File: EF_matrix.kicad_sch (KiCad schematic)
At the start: 4 parts, among them J2 Conn_02x05_Counter_Clockwise, U5 ESP32_NODEMCU

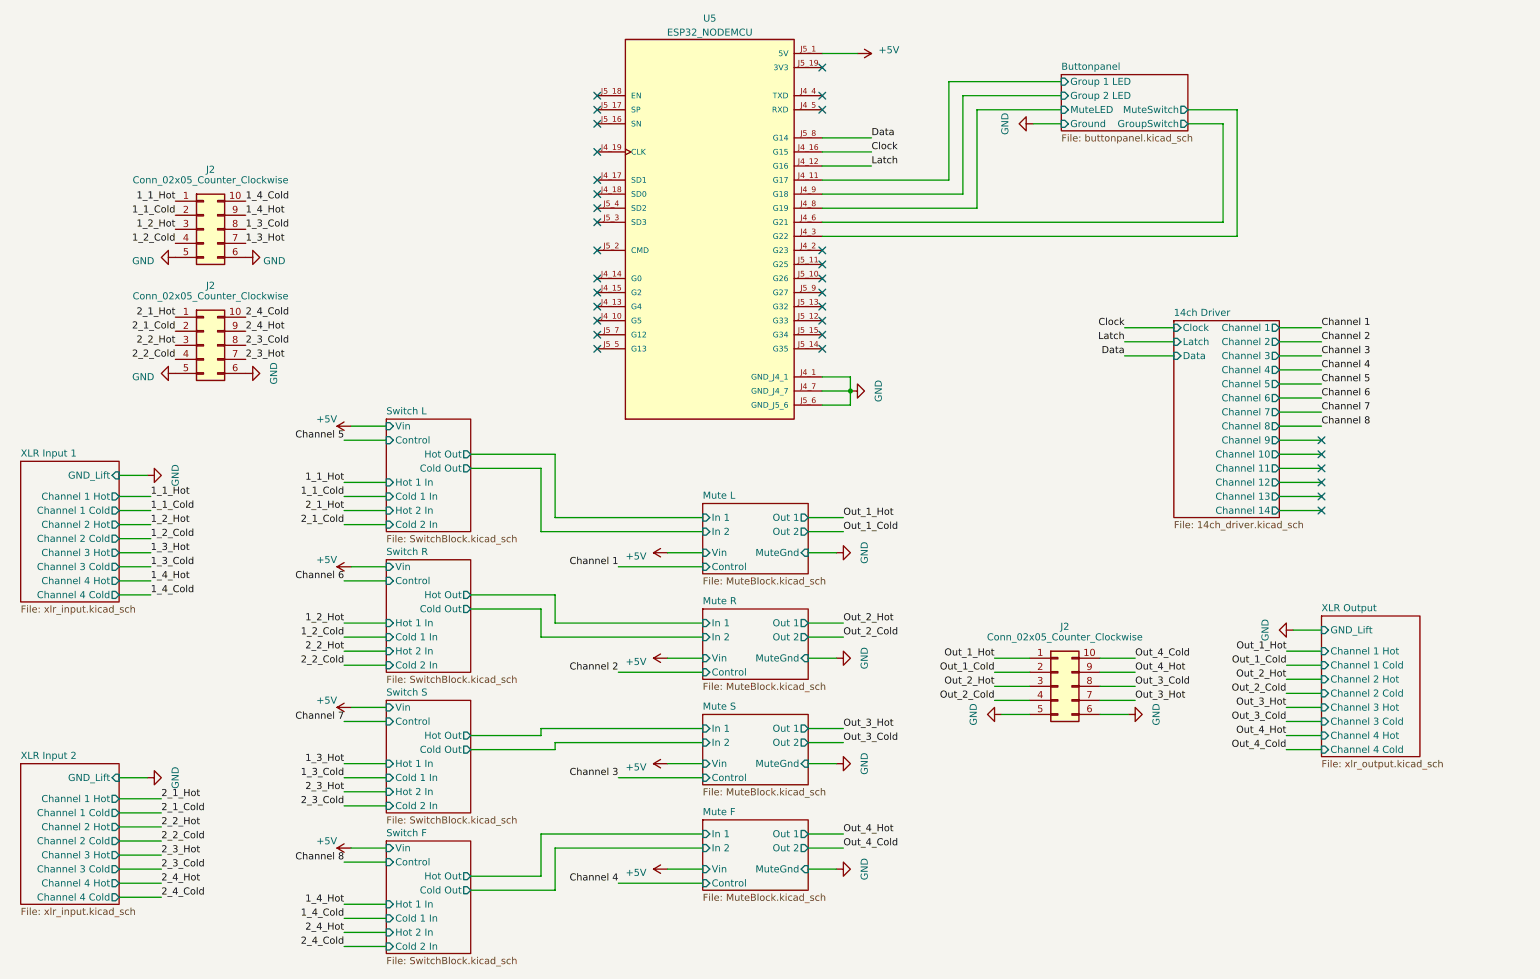
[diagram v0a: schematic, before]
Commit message: Finished up schematic, before board splitting
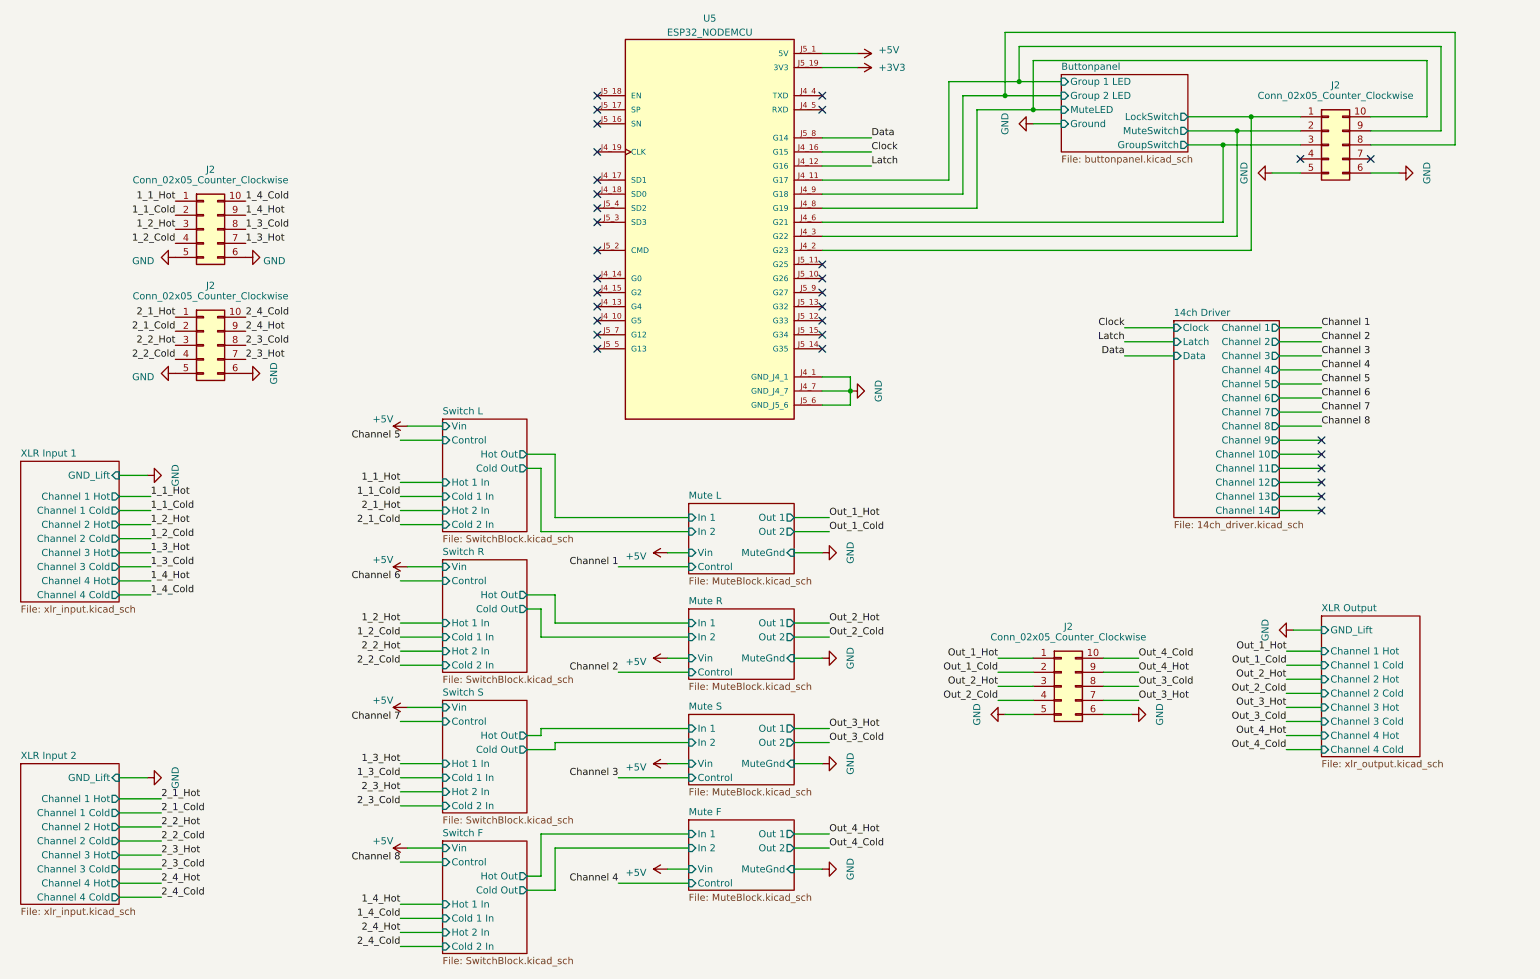
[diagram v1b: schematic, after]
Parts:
- added J2: Conn_02x05_Counter_Clockwise, Connector_PinSocket_2.54mm:PinSocket_2x05_P2.54mm_Vertical, symbol Connector_Generic:Conn_02x05_Counter_Clockwise
- J2: footprint (none) -> Connector_PinSocket_2.54mm:PinSocket_2x05_P2.54mm_Vertical
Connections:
- net Buttonpanel/Group 1 LED: now also J2.9 (Pin_9)
- net Buttonpanel/Group 2 LED: now also J2.8 (Pin_8)
- net Buttonpanel/GroupSwitch: now also J2.3 (Pin_3)
- net Buttonpanel/MuteLED: now also J2.10 (Pin_10)
- net Buttonpanel/MuteSwitch: now also J2.2 (Pin_2)
- net GND: now also J2.5 (Pin_5), J2.6 (Pin_6)
- net Buttonpanel/LockSwitch: now reaches U5.J4_2 (G23)
- net Buttonpanel/LockSwitch: now also J2.1 (Pin_1)
- net +3V3: now reaches U5.J5_19 (3V3)
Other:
- sheet Buttonpanel ports: added LockSwitch; removed none
- moved on the sheet: J2

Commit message: Changed position of ribbon connectors, added DC
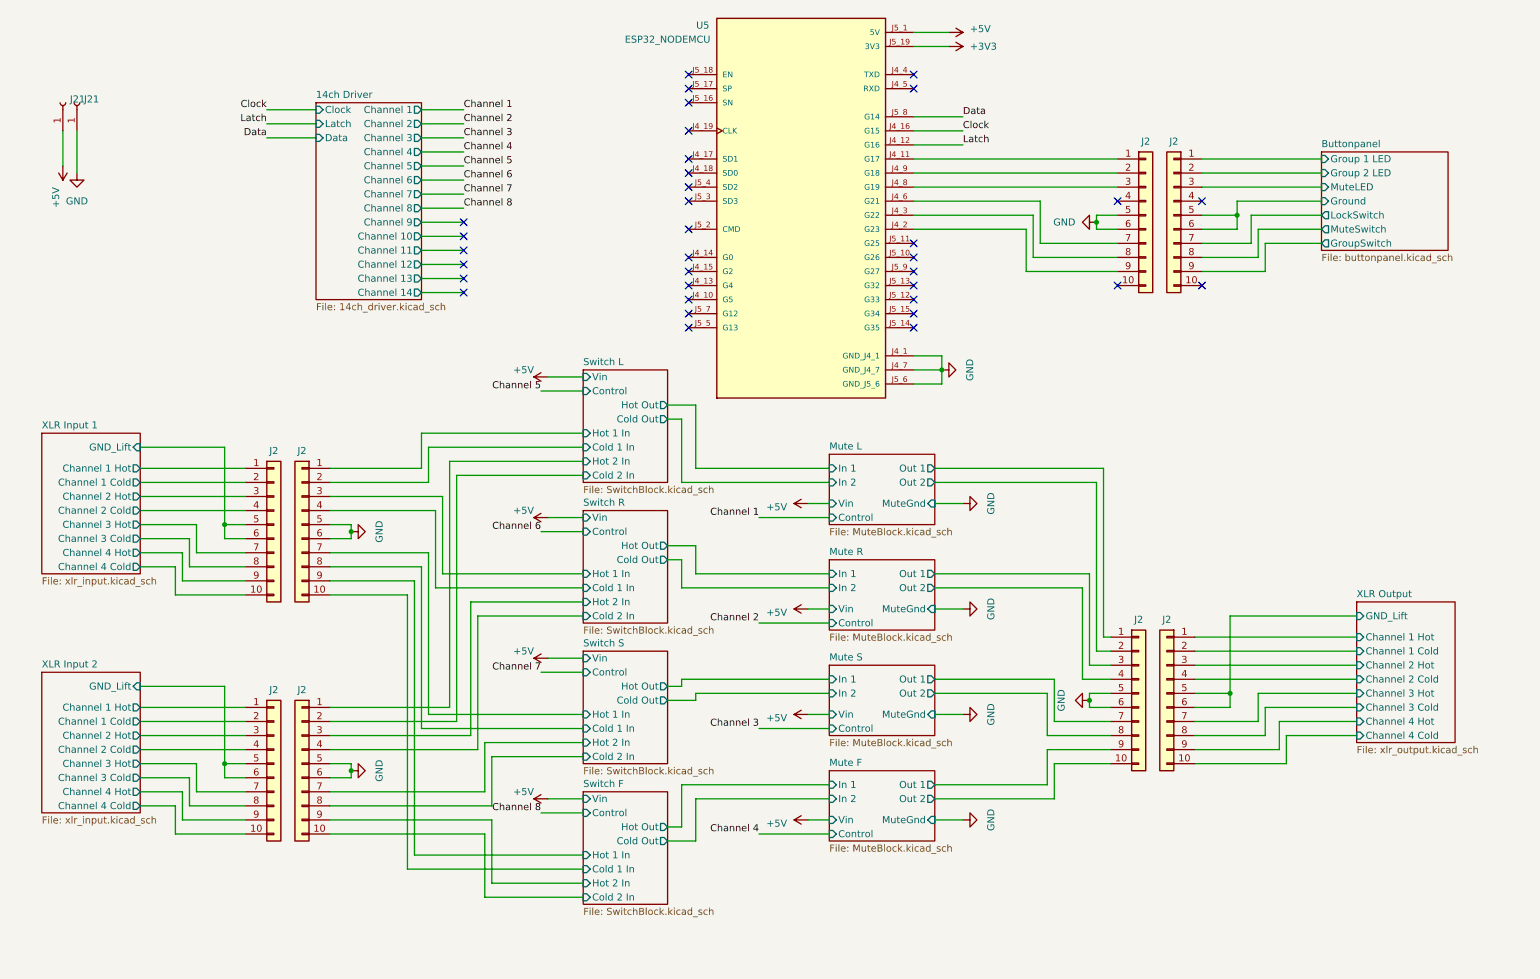
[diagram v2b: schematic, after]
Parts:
- removed J2 (x3): Conn_02x05_Counter_Clockwise, Connector_PinSocket_2.54mm:PinSocket_2x05_P2.54mm_Vertical, symbol Connector_Generic:Conn_02x05_Counter_Clockwise
- added J2 (x7): Conn_02x05_Counter_Clockwise, Connector_PinSocket_2.54mm:PinSocket_2x05_P2.54mm_Vertical, symbol Connector_Generic:Conn_01x10
- added J21 (x2): Conn_01x01_Socket, Connector_Wire:SolderWire-0.75sqmm_1x01_D1.25mm_OD2.3mm, symbol Connector:Conn_01x01_Socket
- J2: symbol Connector_Generic:Conn_02x05_Counter_Clockwise -> Connector_Generic:Conn_01x10
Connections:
- net +5V: now also J21.1 (Pin_1)
- net Buttonpanel/Group 1 LED: now also J2.1 (Pin_1); no longer U5.J4_11 (G17)
- net Buttonpanel/Group 2 LED: now also J2.2 (Pin_2); no longer U5.J4_9 (G18)
- net Buttonpanel/GroupSwitch: now also J2.9 (Pin_9); no longer U5.J4_6 (G21)
- net Buttonpanel/LockSwitch: now also J2.7 (Pin_7); no longer U5.J4_2 (G23)
- net Buttonpanel/MuteLED: now also J2.3 (Pin_3); no longer U5.J4_8 (G19)
- net Buttonpanel/MuteSwitch: now also J2.8 (Pin_8); no longer U5.J4_3 (G22)
- net GND: now also J2.5 (Pin_5), J2.5 (Pin_5), J2.5 (Pin_5), J2.5 (Pin_5), J2.6 (Pin_6), J2.6 (Pin_6), J2.6 (Pin_6), J2.6 (Pin_6), J21.1 (Pin_1); no longer J2.5 (Pin_5), J2.6 (Pin_6)
- net 2_1_Cold renamed XLR Input 1/Channel 1 Cold
- net 2_1_Hot renamed XLR Input 1/Channel 1 Hot
- net 2_2_Cold renamed XLR Input 1/Channel 2 Cold
- net 2_2_Hot renamed XLR Input 1/Channel 2 Hot
- net 2_3_Cold renamed XLR Input 1/Channel 3 Cold
- net 2_3_Hot renamed XLR Input 1/Channel 3 Hot
- net 2_4_Cold renamed XLR Input 1/Channel 4 Cold
- net 2_4_Hot renamed XLR Input 1/Channel 4 Hot
- new net: J2.1 (Pin_1), U5.J4_11 (G17)
- new net: J2.9 (Pin_9), U5.J4_2 (G23)
- new net: J2.8 (Pin_8), U5.J4_3 (G22)
- new net: J2.7 (Pin_7), U5.J4_6 (G21)
- new net: J2.3 (Pin_3), U5.J4_8 (G19)
- new net: J2.2 (Pin_2), U5.J4_9 (G18)
- new net Buttonpanel/Ground: J2.5 (Pin_5), J2.6 (Pin_6)
- new net Mute F/Out 1: J2.9 (Pin_9)
- new net Mute F/Out 2: J2.10 (Pin_10)
- new net Mute L/Out 1: J2.1 (Pin_1)
- new net Mute L/Out 2: J2.2 (Pin_2)
- new net Mute R/Out 1: J2.3 (Pin_3)
- new net Mute R/Out 2: J2.4 (Pin_4)
- new net Mute S/Out 1: J2.7 (Pin_7)
- new net Mute S/Out 2: J2.8 (Pin_8)
- new net Switch F/Cold 1 In: J2.10 (Pin_10)
- new net Switch F/Cold 2 In: J2.10 (Pin_10)
- new net Switch F/Hot 1 In: J2.9 (Pin_9)
- new net Switch F/Hot 2 In: J2.9 (Pin_9)
- new net Switch L/Cold 1 In: J2.2 (Pin_2)
- new net Switch L/Cold 2 In: J2.2 (Pin_2)
- new net Switch L/Hot 1 In: J2.1 (Pin_1)
- new net Switch L/Hot 2 In: J2.1 (Pin_1)
- new net Switch R/Cold 1 In: J2.4 (Pin_4)
- new net Switch R/Cold 2 In: J2.4 (Pin_4)
- new net Switch R/Hot 1 In: J2.3 (Pin_3)
- new net Switch R/Hot 2 In: J2.3 (Pin_3)
- new net Switch S/Cold 1 In: J2.8 (Pin_8)
- new net Switch S/Cold 2 In: J2.8 (Pin_8)
- new net Switch S/Hot 1 In: J2.7 (Pin_7)
- new net Switch S/Hot 2 In: J2.7 (Pin_7)
- new net XLR Input 1/GND_Lift: J2.5 (Pin_5), J2.6 (Pin_6)
- new net XLR Input 2/Channel 1 Cold: J2.2 (Pin_2)
- new net XLR Input 2/Channel 1 Hot: J2.1 (Pin_1)
- new net XLR Input 2/Channel 2 Cold: J2.4 (Pin_4)
- new net XLR Input 2/Channel 2 Hot: J2.3 (Pin_3)
- new net XLR Input 2/Channel 3 Cold: J2.8 (Pin_8)
- new net XLR Input 2/Channel 3 Hot: J2.7 (Pin_7)
- new net XLR Input 2/Channel 4 Cold: J2.10 (Pin_10)
- new net XLR Input 2/Channel 4 Hot: J2.9 (Pin_9)
- new net XLR Input 2/GND_Lift: J2.5 (Pin_5), J2.6 (Pin_6)
- new net XLR Output/Channel 1 Cold: J2.2 (Pin_2)
- new net XLR Output/Channel 1 Hot: J2.1 (Pin_1)
- new net XLR Output/Channel 2 Cold: J2.4 (Pin_4)
- new net XLR Output/Channel 2 Hot: J2.3 (Pin_3)
- new net XLR Output/Channel 3 Cold: J2.8 (Pin_8)
- new net XLR Output/Channel 3 Hot: J2.7 (Pin_7)
- new net XLR Output/Channel 4 Cold: J2.10 (Pin_10)
- new net XLR Output/Channel 4 Hot: J2.9 (Pin_9)
- new net XLR Output/GND_Lift: J2.5 (Pin_5), J2.6 (Pin_6)
- no-connect marks 32 -> 34
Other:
- company: (none) -> Daniel Machnik Sounddesign und Tontechnik
- title: (none) -> Essigfabrik 2-Way PA Switcher
- moved on the sheet: J2, U5

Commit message: Small fixes, schmeatic complete
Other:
- note added: "5V DC Input"
- note added: "Button & LED Panel"
- note added: "Input Panels"
- note added: "Muting"
- note added: "Output Panel"
- note added: "Switching"
